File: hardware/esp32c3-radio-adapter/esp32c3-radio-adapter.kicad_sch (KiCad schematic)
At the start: 10 parts, among them J1 Conn_01x08, J2 Conn_01x08, J3 E07-M1101D_or_Ra-02, J4 Expansion

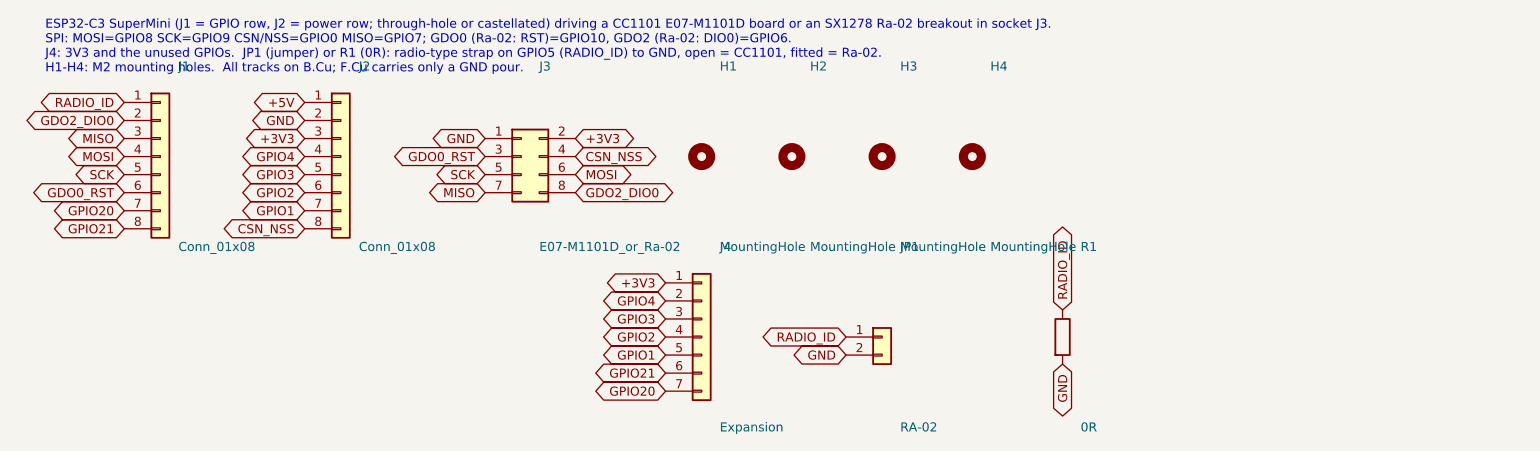
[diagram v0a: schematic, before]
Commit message: Adapters: GPIO map that lets the same socket take all three radio boards
The green D-Sun CC1101 board plugs into the socket adapter's 2x4 socket
too; only its signal order differs, which the firmware absorbs with a pin
map per board.  What the hardware must guarantee is that no socket
position that carries a radio OUTPUT on any of the boards is an ESP32-C3
boot strapping pin (GPIO2/8/9).  Only position 4 (blue CSN, green SCK,
Ra-02 NSS) is an input on every board, so it takes GPIO9; GPIO8 moves to
the spare header and positions 5 and 6 are fed from GPIO3 and GPIO4.

Socket positions 3..8 are now GPIO10, 9, 3, 4, 7, 6.  Per-board maps:
blue E07 MOSI 4 SCK 3 CSN 9 MISO 7 GDO0 10 GDO2 6; green D-Sun MOSI 10
SCK 9 CSN 6 MISO 3 GDO0 7 GDO2 4; Ra-02 MOSI 4 SCK 3 NSS 9 MISO 7 RST 10
DIO0 6.  The README also describes telling the two CC1101 boards apart
passively at power-up (an unconfigured CC1101 clocks XOSC/192 out of
GDO0, on GPIO10 for the blue board and GPIO7 for the green).

Socket adapter routing, still entirely on the back copper: GPIO9 leaves
its pad sideways into the gap before GPIO10 and drops into position 4;
MISO takes the column under GPIO8's pad; SCK and MOSI come down from the
power row through the gaps either side of GPIO8's pad, and GPIO8 climbs
between them to the header (now 3V3, 8, 2, 1, 0, 21TX, 20RX).

SX1278 module adapter: same GPIOs with MOSI and SCK swapped (GPIO3/4) so
its bottom copper nests, NSS on GPIO9 via the top-copper bus, RESET on
GPIO8 (an ESP32 output).

Jumper-wire diagrams: one layout serves all three boards; GPIO4 and GPIO3
take the ribbon's white and black; the Ra-02 strap goes to GPIO1 (GPIO4
is now MOSI).  Both adapters pass ERC and DRC.

Co-Authored-By: Claude Fable 5.1 <noreply@anthropic.com>
Claude-Session: https://claude.ai/code/session_01JoGdh4Cg3VtTTDZi4gQuiN
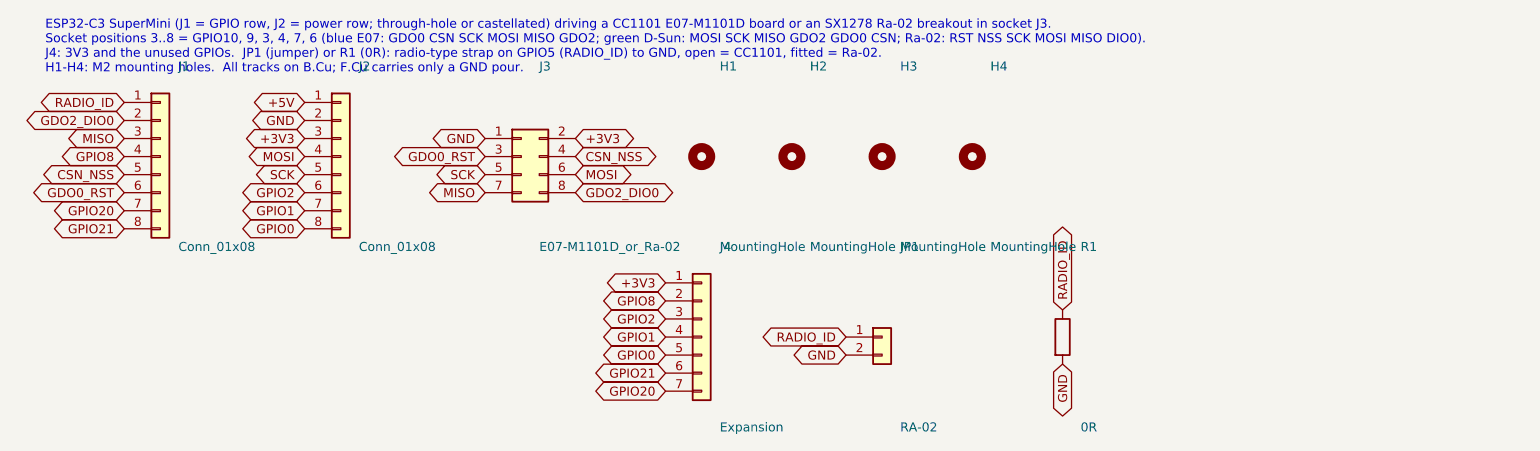
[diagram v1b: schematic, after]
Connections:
- net CSN_NSS: now also J1.5 (Pin_5); no longer J2.8 (Pin_8)
- net GPIO1: now also J4.4 (Pin_4); no longer J4.5 (Pin_5)
- net GPIO2: now also J4.3 (Pin_3); no longer J4.4 (Pin_4)
- net MOSI: now also J2.4 (Pin_4); no longer J1.4 (Pin_4)
- net SCK: now also J2.5 (Pin_5); no longer J1.5 (Pin_5)
- removed net GPIO3: J2.5 (Pin_5), J4.3 (Pin_3)
- net GPIO4 renamed GPIO8
- net GPIO8: now also J1.4 (Pin_4); no longer J2.4 (Pin_4)
- new net GPIO0: J2.8 (Pin_8), J4.5 (Pin_5)
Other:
- note added: "ESP32-C3 SuperMini (J1 = GPIO row, J2 = power row; through-hole or castellated) driving a CC1101 E07-M1101D board or an SX1278 Ra-02 breakout in socket J3. Socket positions 3..8 = GPIO10, 9, 3, 4, 7, 6 (blue E07: GDO0 CSN SCK MOSI MISO GDO2; green D-Sun: MOSI SCK MISO GDO2 GDO0 CSN; Ra-02: RST NSS SCK MOSI MISO DIO0). J4: 3V3 and the unused GPIOs. JP1 (jumper) or R1 (0R): radio-type strap on GPIO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"
- note removed: "ESP32-C3 SuperMini (J1 = GPIO row, J2 = power row; through-hole or castellated) driving a CC1101 E07-M1101D board or an SX1278 Ra-02 breakout in socket J3. SPI: MOSI=GPIO8 SCK=GPIO9 CSN/NSS=GPIO0 MISO=GPIO7; GDO0 (Ra-02: RST)=GPIO10, GDO2 (Ra-02: DIO0)=GPIO6. J4: 3V3 and the unused GPIOs. JP1 (jumper) or R1 (0R): radio-type strap on GPIO5 (RADIO_ID) to GND, open = CC1101, fitted = Ra-02. H1-H4: M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"
- title: ESP32-C3 SuperMini to CC1101 (E07-M1101D) or SX1278 Ra-02 breakout adapter -> ESP32-C3 SuperMini to CC1101 (E07-M1101D, D-Sun) or SX1278 Ra-02 breakout adapter
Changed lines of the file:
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@@
 	(paper "A4")
 	(title_block
-		(title "ESP32-C3 SuperMini to CC1101 (E07-M1101D) or SX1278 Ra-02 breakout adapter")
+		(title "ESP32-C3 SuperMini to CC1101 (E07-M1101D, D-Sun) or SX1278 Ra-02 breakout adapter")
 		(rev "${GIT_DESCRIBE}")
-		(comment 1 "Carrier joining an ESP32-C3 SuperMini to an Ebyte E07-M1101D-SMA CC1101 board or an SX1278 Ra-02 breakout via one 2x4 socket; all tracks on the back, GND pour on the front")
+		(comment 1 "Carrier joining an ESP32-C3 SuperMini to a CC1101 board (Ebyte E07-M1101D-SMA or D-Sun) or an SX1278 Ra-02 breakout via one 2x4 socket; all tracks on the back, GND pour on the front")
 	)
 	(symbol
@@
 		)
 	)
-	(global_label "MOSI"
+	(global_label "GPIO8"
 		(shape bidirectional)
 		(at 71.12 101.6 180)
@@
 		)
 	)
-	(global_label "SCK"
+	(global_label "CSN_NSS"
 		(shape bidirectional)
 		(at 71.12 104.14 180)
@@
 		)
 	)
-	(global_label "GPIO4"
+	(global_label "MOSI"
 		(shape bidirectional)
 		(at 96.52 101.6 180)
@@
 		)
 	)
-	(global_label "GPIO3"
+	(global_label "SCK"
 		(shape bidirectional)
 		(at 96.52 104.14 180)
@@
 		)
 	)
-	(global_label "CSN_NSS"
+	(global_label "GPIO0"
 		(shape bidirectional)
 		(at 96.52 111.76 180)
@@
 		)
 	)
-	(global_label "GPIO4"
+	(global_label "GPIO8"
 		(shape bidirectional)
 		(at 147.32 121.92 180)
@@
 		)
 	)
-	(global_label "GPIO3"
+	(global_label "GPIO2"
 		(shape bidirectional)
 		(at 147.32 124.46 180)
@@
 		)
 	)
-	(global_label "GPIO2"
+	(global_label "GPIO1"
 		(shape bidirectional)
 		(at 147.32 127 180)
@@
 		)
 	)
-	(global_label "GPIO1"
+	(global_label "GPIO0"
 		(shape bidirectional)
 		(at 147.32 129.54 180)
@@
 		)
 	)
-	(text "ESP32-C3 SuperMini (J1 = GPIO row, J2 = power row; through-hole or castellated) driving a CC1101 E07-M1101D board or an SX1278 Ra-02 breakout in socket J3.\nSPI: MOSI=GPIO8 SCK=GPIO9 CSN/NSS=GPIO0 MISO=GPIO7; GDO0 (Ra-02: RST)=GPIO10, GDO2 (Ra-02: DIO0)=GPIO6.\nJ4: 3V3 and the unused GPIOs.  JP1 (jumper) or R1 (0R): radio-type strap on GPIO5 (RADIO_ID) to GND, open = CC1101, fitted = Ra-02.\nH1-H4: M2 mounting holes.  All tracks on B.Cu; F.Cu carries only a GND pour."
+	(text "ESP32-C3 SuperMini (J1 = GPIO row, J2 = power row; through-hole or castellated) driving a CC1101 E07-M1101D board or an SX1278 Ra-02 breakout in socket J3.\nSocket positions 3..8 = GPIO10, 9, 3, 4, 7, 6 (blue E07: GDO0 CSN SCK MOSI MISO GDO2; green D-Sun: MOSI SCK MISO GDO2 GDO0 CSN; Ra-02: RST NSS SCK MOSI MISO DIO0).\nJ4: 3V3 and the unused GPIOs.  JP1 (jumper) or R1 (0R): radio-type strap on GPIO5 (RADIO_ID) to GND, open = CC1101, fitted = Ra-02.\nH1-H4: M2 mounting holes.  All tracks on B.Cu; F.Cu carries only a GND pour."
 		(exclude_from_sim no)
 		(at 60 90 0)

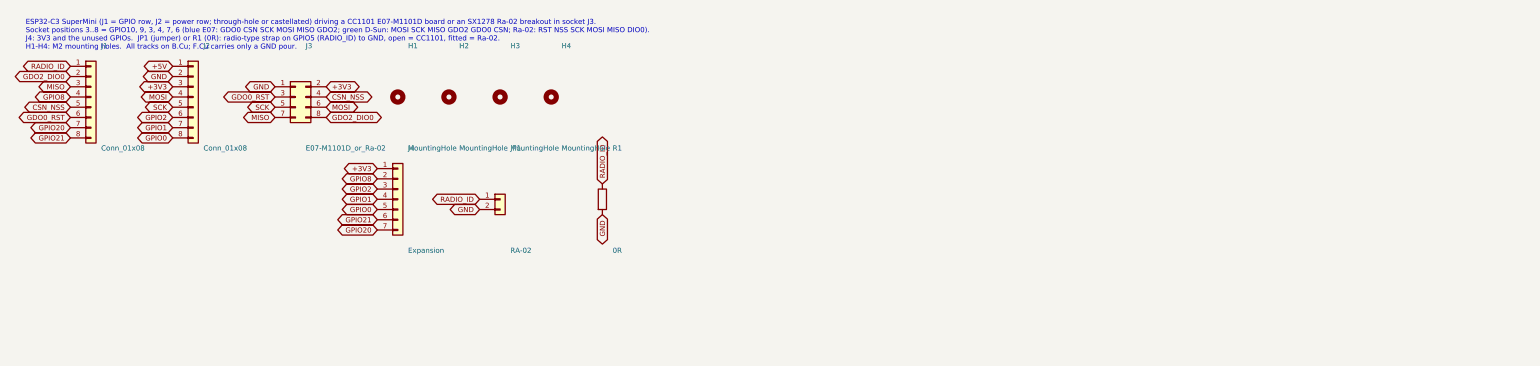
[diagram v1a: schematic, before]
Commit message: Socket adapter: move CSN/NSS off the GPIO9 boot strap to GPIO1
On the bench (2026-09-06) the CC1101/Ra-02 nodes powered straight into USB
download mode every reset and never ran the firmware.  Root cause: socket
position 4 (CSN on the blue board, SCK on the green, NSS on the Ra-02) was
GPIO9, the ESP32-C3 BOOT strap.  A radio pin loads that net with enough
capacitance that, through the chip's weak internal pull-up, it rises too
slowly for the mask ROM to read it high at reset, so the ROM latches BOOT low
and enters download mode.  It is not the firmware -- the ROM samples the strap
before any code runs -- and it is not fixable in software.

Fix, single layer as before: position 4 now takes GPIO1 (routed from the power
row, across between the SuperMini rows and into the pad from the left).  GPIO9
is left unconnected -- an unconnected strap floats high on the internal
pull-up, the safest state -- so the socket now carries no strap at all.  The
expansion header keeps its proven 7-pin geometry: GPIO1's old slot becomes a
second 3V3, and GPIO8/GPIO2 (the straps that stay exposed there) each get an
optional do-not-populate pull-up-to-3V3 footprint (R2/R3) bridging to the
adjacent 3V3 pin.  ERC/DRC clean.

Firmware pin map changes by one pin only: CSN/SCK/NSS 9 -> 1; everything else
unchanged.

Co-Authored-By: Claude Opus 4.8 <noreply@anthropic.com>
Claude-Session: https://claude.ai/code/session_01JoGdh4Cg3VtTTDZi4gQuiN
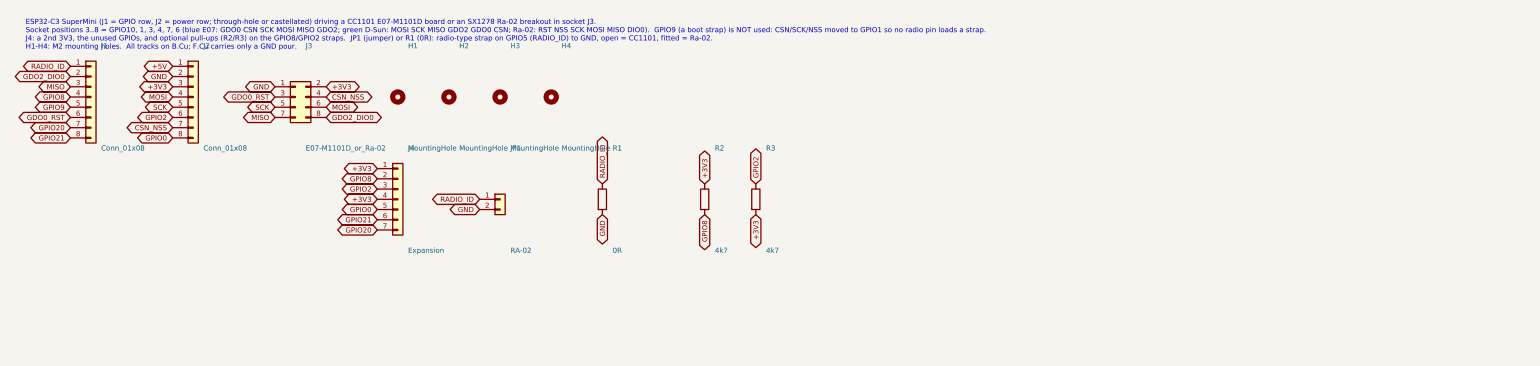
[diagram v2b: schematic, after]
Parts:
- added R2, R3: 4k7, Adapter:R_0805_HeaderPullup, symbol Device:R
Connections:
- net +3V3: now also J4.4 (Pin_4), R2.1, R3.2
- net CSN_NSS: now also J2.7 (Pin_7); no longer J1.5 (Pin_5)
- net GPIO2: now also R3.1
- net GPIO8: now also R2.2
- removed net GPIO1: J2.7 (Pin_7), J4.4 (Pin_4)
- new net GPIO9: J1.5 (Pin_5)
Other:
- note added: "ESP32-C3 SuperMini (J1 = GPIO row, J2 = power row; through-hole or castellated) driving a CC1101 E07-M1101D board or an SX1278 Ra-02 breakout in socket J3. Socket positions 3..8 = GPIO10, 1, 3, 4, 7, 6 (blue E07: GDO0 CSN SCK MOSI MISO GDO2; green D-Sun: MOSI SCK MISO GDO2 GDO0 CSN; Ra-02: RST NSS SCK MOSI MISO DIO0). GPIO9 (a boot strap) is NOT used: CSN/SCK/NSS moved to GPIO1 so no radio pin lo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"
- note removed: "ESP32-C3 SuperMini (J1 = GPIO row, J2 = power row; through-hole or castellated) driving a CC1101 E07-M1101D board or an SX1278 Ra-02 breakout in socket J3. Socket positions 3..8 = GPIO10, 9, 3, 4, 7, 6 (blue E07: GDO0 CSN SCK MOSI MISO GDO2; green D-Sun: MOSI SCK MISO GDO2 GDO0 CSN; Ra-02: RST NSS SCK MOSI MISO DIO0). J4: 3V3 and the unused GPIOs. JP1 (jumper) or R1 (0R): radio-type strap on GPIO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"
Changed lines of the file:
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@@
 		)
 	)
-	(global_label "CSN_NSS"
+	(global_label "GPIO9"
 		(shape bidirectional)
 		(at 71.12 104.14 180)
@@
 		)
 	)
-	(global_label "GPIO1"
+	(global_label "CSN_NSS"
 		(shape bidirectional)
 		(at 96.52 109.22 180)
@@
 		)
 	)
-	(global_label "GPIO1"
+	(global_label "+3V3"
 		(shape bidirectional)
 		(at 147.32 127 180)
@@
 	)
 	(symbol
+		(lib_id "Device:R")
+		(at 228.6 127 0)
+		(unit 1)
+		(exclude_from_sim no)
+		(in_bom yes)
+		(on_board yes)
+		(dnp no)
+		(fields_autoplaced yes)
+		(property "Reference" "R2"
+			(at 231.14 114.3 0)
+			(effects
+				(font
+					(size 1.27 1.27)
+				)
+				(justify left)
+			)
+		)
+		(property "Value" "4k7"
+			(at 231.14 139.7 0)
+			(effects
+				(font
+					(size 1.27 1.27)
+				)
+				(justify left)
+			)
+		)
+		(property "Footprint" "Adapter:R_0805_HeaderPullup"
+			(at 228.6 127 0)
+			(effects
+				(font
+					(size 1.27 1.27)
+				)
+				(hide yes)
+			)
+		)
+		(property "Datasheet" "~"
+			(at 228.6 127 0)
+			(effects
+				(font
+					(size 1.27 1.27)
+				)
+				(hide yes)
+			)
+		)
+		(property "Description" "Optional pull-up: GPIO8 boot strap to 3V3 (DNP unless needed)"
+			(at 228.6 127 0)
+			(effects
+				(font
+					(size 1.27 1.27)
+				)
+				(hide yes)
+			)
+		)
+		(pin "1"
+		)
+		(pin "2"
+		)
+		(instances
+			(project "esp32c3-radio-adapter"
+				(path "/b71943b6-a88f-5429-bfd6-fb1a52f93b27"
+					(reference "R2")
+					(unit 1)
+				)
+			)
+		)
+	)
+	(global_label "+3V3"
+		(shape bidirectional)
+		(at 228.6 123.19 90)
+		(fields_autoplaced yes)
+		(effects
+			(font
+				(size 1.27 1.27)
+			)
+			(justify left)
+		)
+		(property "Intersheetrefs" "${INTERSHEET_REFS}"
+			(at 228.6 123.19 0)
+			(effects
+				(font
+					(size 1.27 1.27)
+				)
+				(justify left)
+				(hide yes)
+			)
+		)
+	)
+	(global_label "GPIO8"
+		(shape bidirectional)
+		(at 228.6 130.81 270)
+		(fields_autoplaced yes)
+		(effects
+			(font
+				(size 1.27 1.27)
+			)
+			(justify right)
+		)
+		(property "Intersheetrefs" "${INTERSHEET_REFS}"
+			(at 228.6 130.81 0)
+			(effects
+				(font
+					(size 1.27 1.27)
+				)
+				(justify right)
+				(hide yes)
+			)
+		)
+	)
+	(symbol
+		(lib_id "Device:R")
+		(at 241.3 127 0)
+		(unit 1)
+		(exclude_from_sim no)
+		(in_bom yes)
+		(on_board yes)
+		(dnp no)
+		(fields_autoplaced yes)
+		(property "Reference" "R3"
+			(at 243.84 114.3 0)
+			(effects
+				(font
+					(size 1.27 1.27)
+				)
+				(justify left)
+			)
+		)
+		(property "Value" "4k7"
+			(at 243.84 139.7 0)
+			(effects
+				(font
+					(size 1.27 1.27)
+				)
+				(justify left)
+			)
+		)
+		(property "Footprint" "Adapter:R_0805_HeaderPullup"
+			(at 241.3 127 0)
+			(effects
+				(font
+					(size 1.27 1.27)
+				)
+				(hide yes)
+			)
+		)
+		(property "Datasheet" "~"
+			(at 241.3 127 0)
+			(effects
+				(font
+					(size 1.27 1.27)
+				)
+				(hide yes)
+			)
+		)
+		(property "Description" "Optional pull-up: GPIO2 boot strap to 3V3 (DNP unless needed)"
+			(at 241.3 127 0)
+			(effects
+				(font
+					(size 1.27 1.27)
+				)
+				(hide yes)
+			)
+		)
+		(pin "1"
+		)
+		(pin "2"
+		)
+		(instances
+			(project "esp32c3-radio-adapter"
+				(path "/b71943b6-a88f-5429-bfd6-fb1a52f93b27"
+					(reference "R3")
+					(unit 1)
+				)
+			)
+		)
+	)
+	(global_label "GPIO2"
+		(shape bidirectional)
+		(at 241.3 123.19 90)
+		(fields_autoplaced yes)
+		(effects
+			(font
+				(size 1.27 1.27)
+			)
+			(justify left)
+		)
+		(property "Intersheetrefs" "${INTERSHEET_REFS}"
+			(at 241.3 123.19 0)
+			(effects
+				(font
+					(size 1.27 1.27)
+				)
+				(justify left)
+				(hide yes)
+			)
+		)
+	)
+	(global_label "+3V3"
+		(shape bidirectional)
+		(at 241.3 130.81 270)
+		(fields_autoplaced yes)
+		(effects
+			(font
+				(size 1.27 1.27)
+			)
+			(justify right)
+		)
+		(property "Intersheetrefs" "${INTERSHEET_REFS}"
+			(at 241.3 130.81 0)
+			(effects
+				(font
+					(size 1.27 1.27)
+				)
+				(justify right)
+				(hide yes)
+			)
+		)
+	)
+	(symbol
 		(lib_id "Mechanical:MountingHole")
 		(at 152.4 101.6 0)
@@
 		)
 	)
-	(text "ESP32-C3 SuperMini (J1 = GPIO row, J2 = power row; through-hole or castellated) driving a CC1101 E07-M1101D board or an SX1278 Ra-02 breakout in socket J3.\nSocket positions 3..8 = GPIO10, 9, 3, 4, 7, 6 (blue E07: GDO0 CSN SCK MOSI MISO GDO2; green D-Sun: MOSI SCK MISO GDO2 GDO0 CSN; Ra-02: RST NSS SCK MOSI MISO DIO0).\nJ4: 3V3 and the unused GPIOs.  JP1 (jumper) or R1 (0R): radio-type strap on GPIO5 (RADIO_ID) to GND, open = CC1101, fitted = Ra-02.\nH1-H4: M2 mounting holes.  All tracks on B.Cu; F.Cu carries only a GND pour."
+	(text "ESP32-C3 SuperMini (J1 = GPIO row, J2 = power row; through-hole or castellated) driving a CC1101 E07-M1101D board or an SX1278 Ra-02 breakout in socket J3.\nSocket positions 3..8 = GPIO10, 1, 3, 4, 7, 6 (blue E07: GDO0 CSN SCK MOSI MISO GDO2; green D-Sun: MOSI SCK MISO GDO2 GDO0 CSN; Ra-02: RST NSS SCK MOSI MISO DIO0).  GPIO9 (a boot strap) is NOT used: CSN/SCK/NSS moved to GPIO1 so no radio pin loads a strap.\nJ4: a 2nd 3V3, the unused GPIOs, and optional pull-ups (R2/R3) on the GPIO8/GPIO2 straps.  JP1 (jumper) or R1 (0R): radio-type strap on GPIO5 (RADIO_ID) to GND, open = CC1101, fitted = Ra-02.\nH1-H4: M2 mounting holes.  All tracks on B.Cu; F.Cu carries only a GND pour."
 		(exclude_from_sim no)
 		(at 60 90 0)
